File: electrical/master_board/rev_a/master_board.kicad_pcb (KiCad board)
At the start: 2 copper layers, 145.3 x 156.6 mm, 181 parts, among them CN1 USB3140-30-230-1-C;VERT,2.3FL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, CN10 WOW_OUT;M2x6S, CN2 USB3140-30-230-1-C;VERT,2.3FL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, CN5 LIDAR_ADAPTER;2xF1x3+F1x2, CN6 SERVO;F1x3, CN7 SERVO;F1x3, CN8 SERVO;F1x3, CN81 HCSR04LP;F1X4, CN82 HCSR04LP;F1X4, CN83 HCSR04LP;F1X4, CN84 HCSR04LP;F1X4, CN85 HCSR04LP;F1X4, CN86 HCSR04LP;F1X4, CN87 HCSR04LP;F1X4, CN88 MIKROBUS_MATE;SMALL, CN89 MIKROBUS_MATE;MEDIUM, CN9 SERVO;F1x3, CN90 STADAPTER;F2x4, CN91 HR2_ENCODER;2xF1x3, CN92 HR2_ENCODER;2xF1x3, CN93 POLOLU_U3V70F9;F1x4+F1x5, CN94 RASPI;F2X20, CN95 NUCLEO-F767ZI;2xF2x35, Q1 2N2222;SOT23, Q10 2N7000;SOT23, Q11 2N7000;SOT23, Q12 2N7000;SOT23, Q13 2N7000;SOT23, Q14 2N7000;SOT23, Q15 2N7000;SOT23, Q16 2N7000;SOT23, Q17 2N7000;SOT23, Q18 2N7000;SOT23, Q19 2N7000;SOT23, Q2 POWER_PFET_GSD, Q20 2N7000;SOT23, Q21 PFET_6A_GSD;SOT23, Q22 2N7000;SOT23, Q3 2N2222;SOT23, Q4 2N7000;SOT23, Q5 2N7000;SOT23, Q6 2N7000;SOT23, Q7 2N7000;SOT23, Q8 2N7000;SOT23, Q9 2N7000;SOT23, SW1 BUTTON;6x3.5, SW2 BUTTON;6x3.5, SW3 BUTTON;6x3.5, U1 LM66100;SOT363, U10 CD450B;TTSOP16, U11 SN74HCS595;TTSOP16, U12 SN74HCS595;TTSOP16, U13 74LVC1G11;SOT363, U14 MCP2542;SOIC8, U15 MCP2542;SOIC8, U16 74LVC1G74;TSSOP8, U17 CPC1017N;SOP4W3.8L4.1, U18 CPC1017N;SOP4W3.8L4.1, U2 MCP7940;SOIC8, U3 CAT24C32;SOIC8, U4 DRV8833PWPR;16HTSSOP, U5 SN74HCS595;TTSOP16, U6 SN74HCS166;TTSOP16, U7 SN74HCS166;TTSOP16, U8 SN74HCS595;TTSOP16, U9 CD450B;TTSOP16, X1 32.768kHz9pF;3.2x1.5

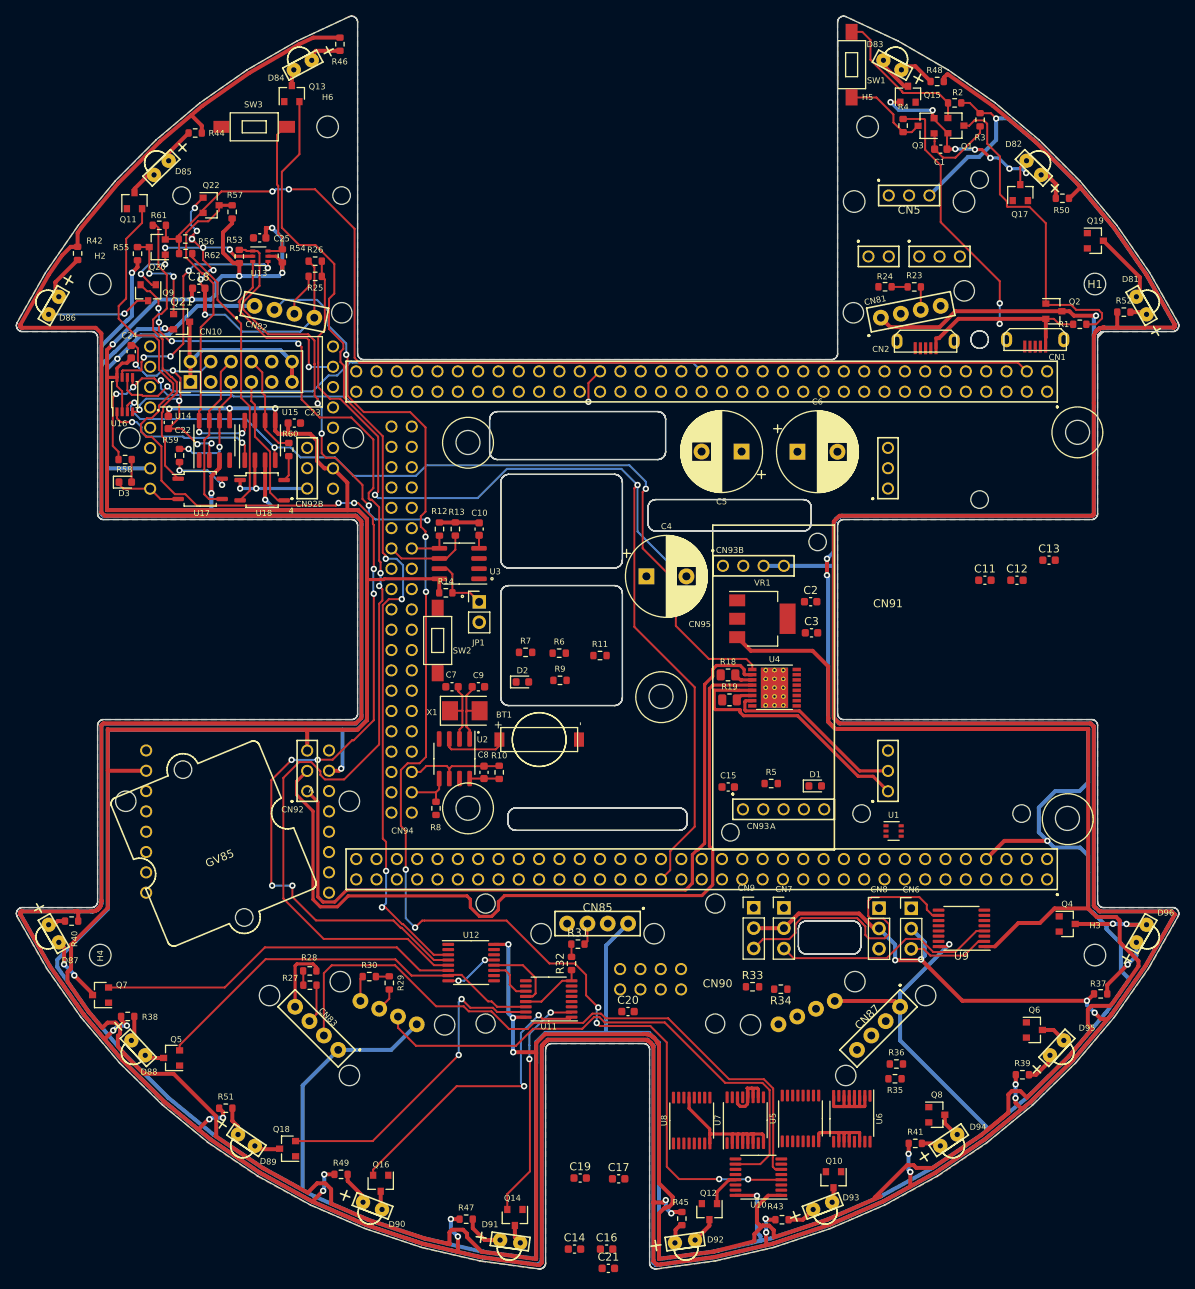
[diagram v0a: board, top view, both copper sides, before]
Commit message: More work on NW quadrant of PCB.
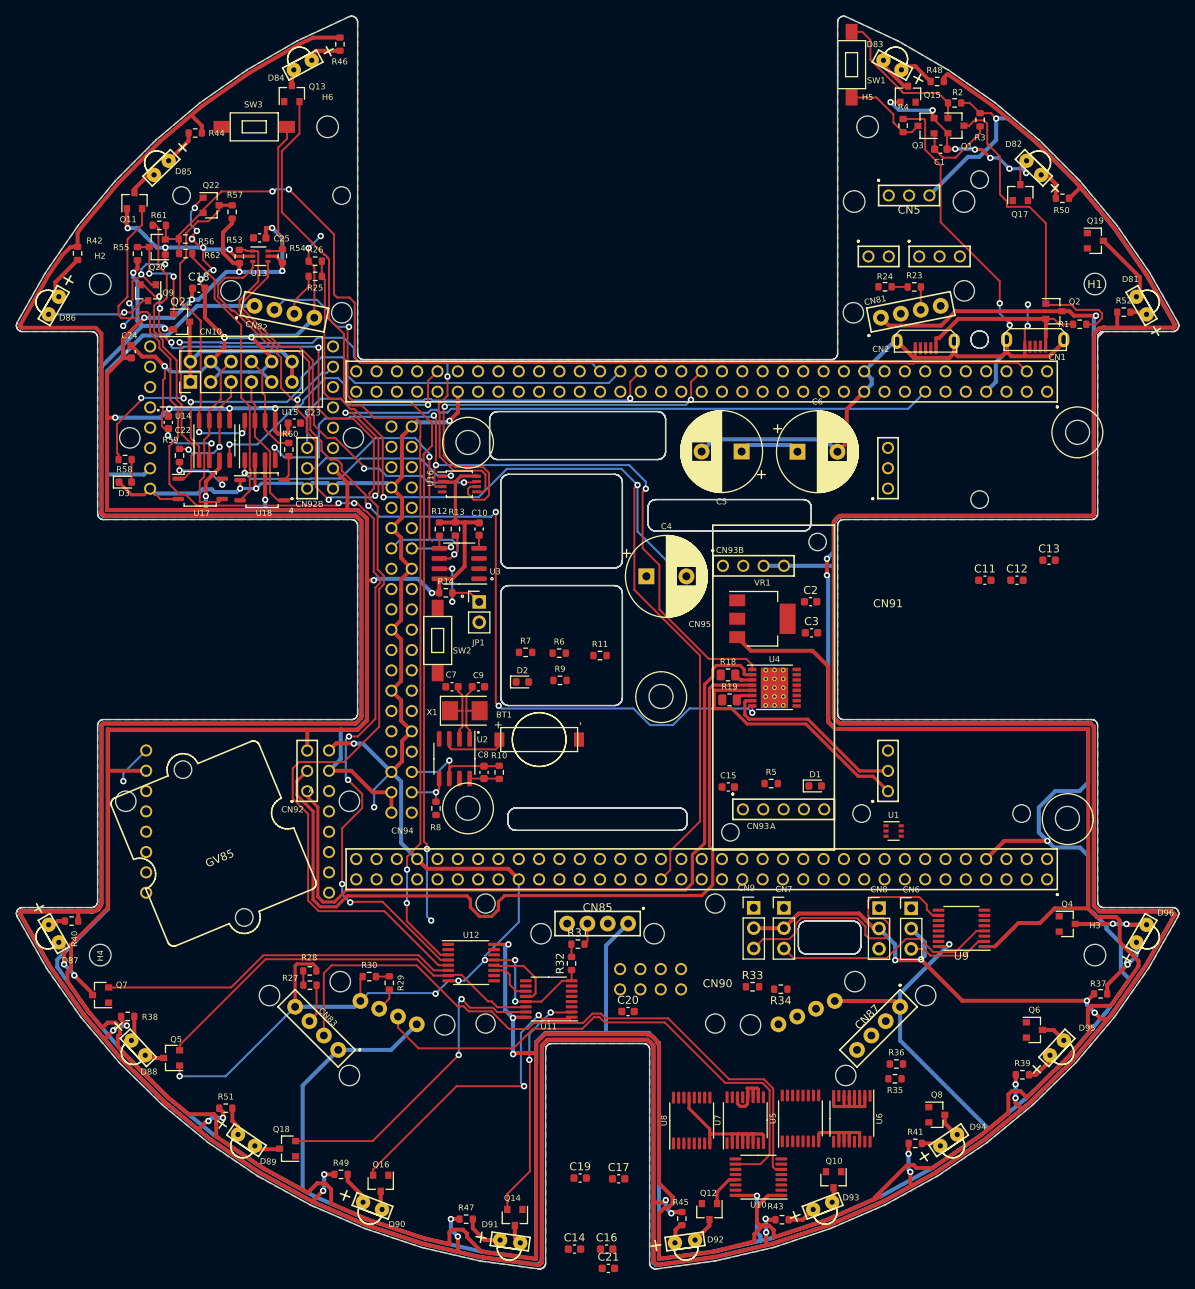
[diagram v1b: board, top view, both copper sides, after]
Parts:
- moved U16 43.3 mm to (82.7, 83.1), turned to 0 degrees
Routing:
- net /GND: track 228.4 -> 531.9 mm, vias 28 -> 42
- net /~NRST: track 23.6 -> 138.1 mm, vias 1 -> 4
- net /Sonars and Servos/TRIG2_5V: track 168.3 -> 95.4 mm, vias 9 -> 3
- net /WOW_TX: track 0.00 -> 67.4 mm, vias 0 -> 1
- net /~MOTOR_FAULT: track 53.8 -> 119.4 mm
- net /WOW_RX: track 0.00 -> 61.6 mm, vias 0 -> 2
- net /LQUAD_A: track 0.00 -> 28.8 mm, vias 0 -> 1
- net /LQUAD_B: track 0.00 -> 25.8 mm, vias 0 -> 1
- net /ESTOP: track 76.2 -> 98.8 mm
- net /~ESTOP_CLR: track 76.5 -> 55.7 mm, vias 1 -> 2
- net /WOWBus/~ESTOP_SET: track 31.2 -> 50.3 mm, vias 4 -> 2
- net /LED's/LED5: track 152.7 -> 138.0 mm, vias 8 -> 6
- net /5V: track 757.2 -> 767.9 mm, vias 11 -> 9
- net /WOWBus/ESTOP_TRIG: track 20.4 -> 30.8 mm
- net /~ESTOP: track 105.7 -> 95.7 mm, vias 3 -> 4
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
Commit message: More pushing and shoving of wires on PCB.
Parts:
- moved R7 7.67 mm to (83.4, 103.0)
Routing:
- net /DIO_MISO: track 0.00 -> 147.2 mm, vias 0 -> 3
- net /~DIO_NSS: track 0.00 -> 115.0 mm, vias 0 -> 4
- net /DIO_SCK: track 0.00 -> 104.4 mm, vias 0 -> 4
- net /ECHO7: track 2.01 -> 96.5 mm, vias 0 -> 4
- net /STL_TX: track 0.00 -> 74.9 mm, vias 0 -> 5
- net /SBC_ALIVE: track 0.00 -> 46.7 mm, vias 0 -> 2
- net /LQUAD_B: track 25.8 -> 66.4 mm
- net /GND: track 531.9 -> 559.4 mm
- net /DIO_MOSI: track 0.00 -> 26.4 mm, vias 0 -> 2
- net /ECHO2: track 134.0 -> 121.3 mm, vias 2 -> 4
- net /5V: track 767.9 -> 780.1 mm
- net /LED's/LED4: track 122.1 -> 126.3 mm, vias 2 -> 4
- net /~MOTOR_FAULT: track 119.4 -> 117.0 mm
- net /Motors_Encoders/LMOTOR_OUT2: track 102.4 -> 100.8 mm
- net /Single Board Computer/ID_SCL: track 15.0 -> 16.4 mm
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
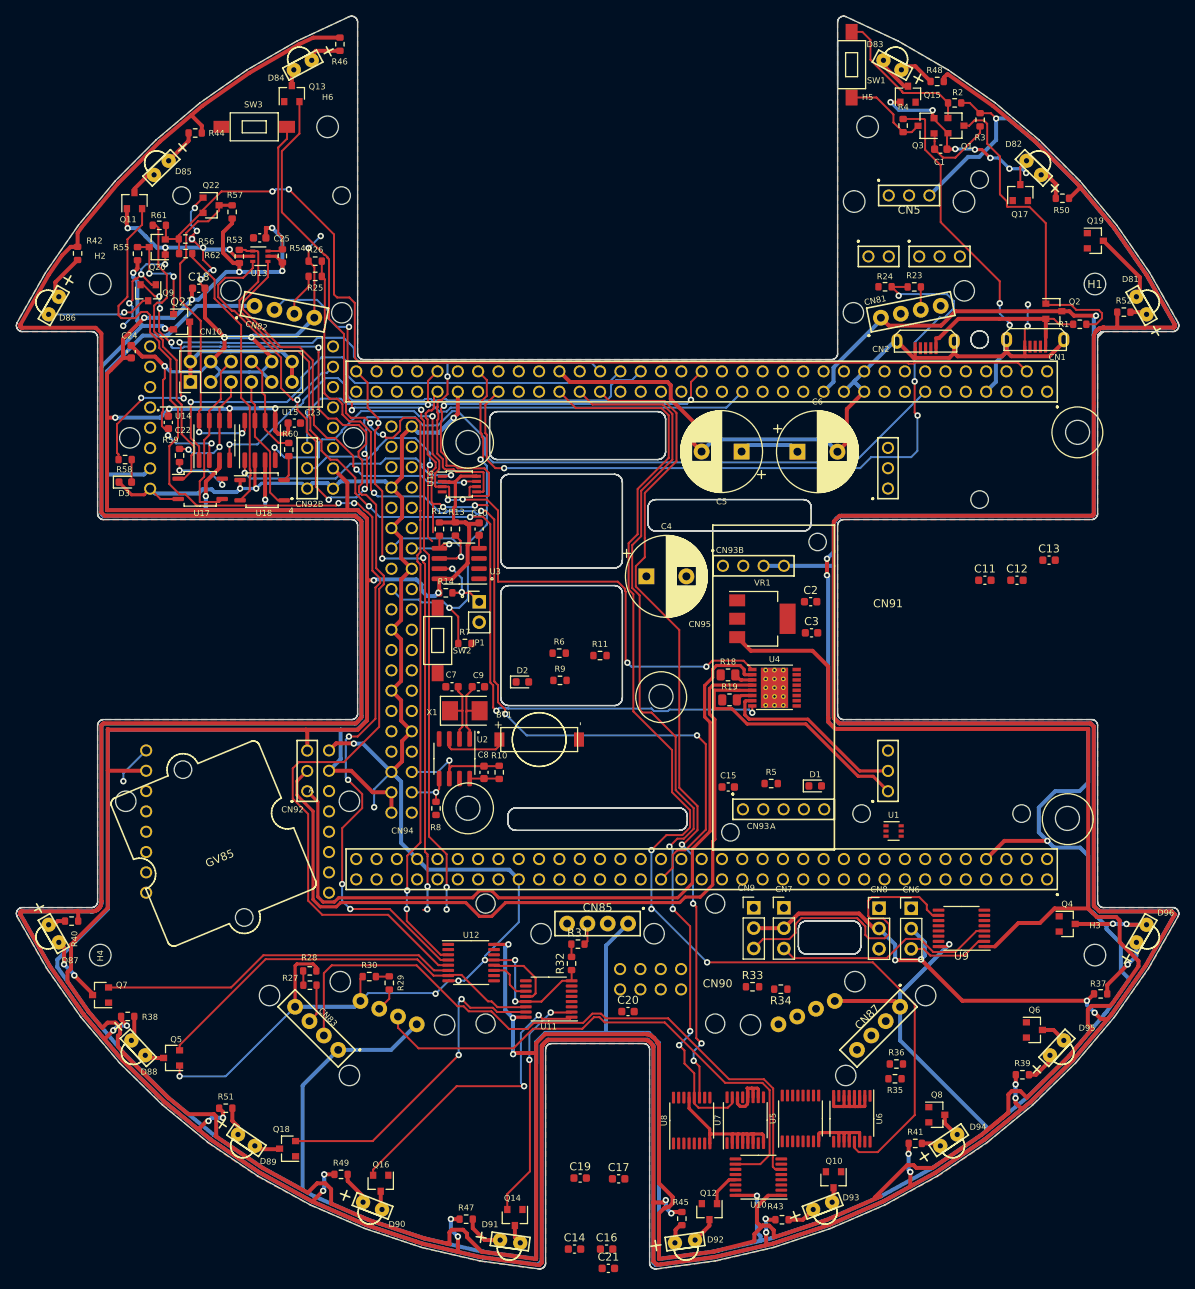
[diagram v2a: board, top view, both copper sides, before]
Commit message: Weaving traces from NE corner around the heat sink holes.
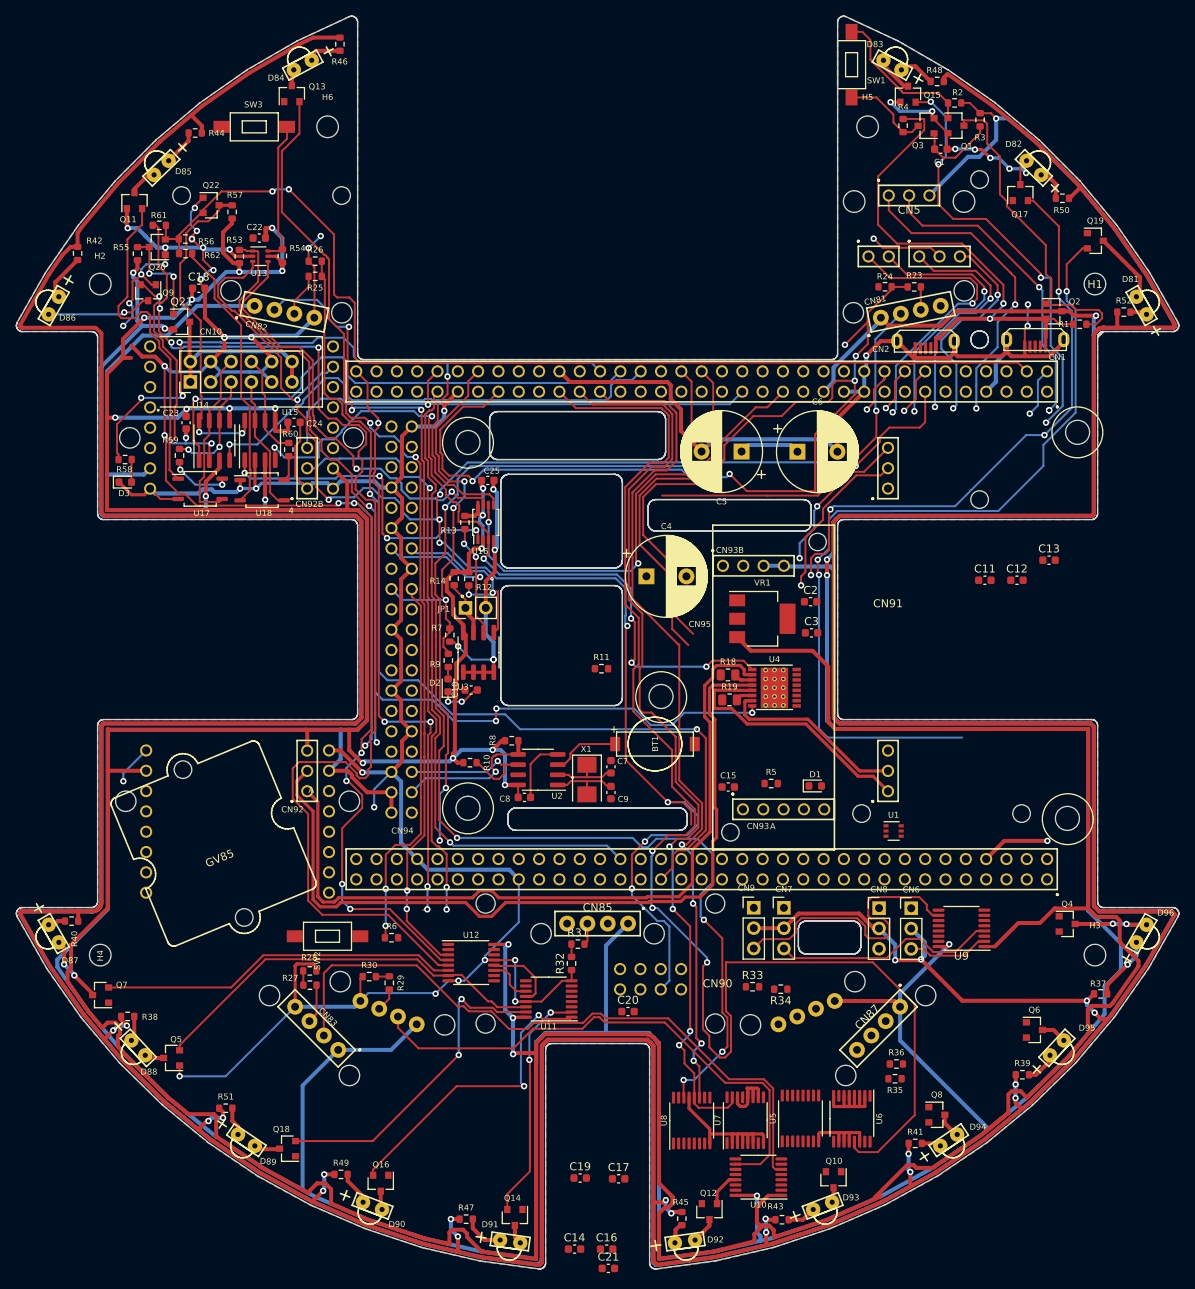
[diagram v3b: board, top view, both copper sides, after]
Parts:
- moved C25 41.6 mm to (86.3, 82.6), turned to 180 degrees
- moved R6 41.3 mm to (74.2, 139.8)
- moved SW2 39.5 mm to (66.2, 139.6), turned to 180 degrees
- moved C22 25.7 mm to (57.7, 52.3), turned to 0 degrees
- moved C7 22.2 mm to (101.7, 118.4), turned to 90 degrees
- moved C24 22.2 mm to (62.0, 75.3), turned to 180 degrees
- moved C9 21.2 mm to (101.7, 121.6), turned to 270 degrees
- moved C10 20.1 mm to (84.2, 108.8), turned to 180 degrees
- moved X1 17.5 mm to (98.7, 120.0), turned to 270 degrees
- moved BT1 14.5 mm to (107.2, 115.6)
- moved R9 14.2 mm to (81.3, 105.1), turned to 270 degrees
- moved C23 13.5 mm to (48.6, 75.4), turned to 90 degrees
- moved R8 12.7 mm to (89.3, 115.2), turned to 0 degrees
- moved U3 11.4 mm to (85.1, 104.1), turned to 90 degrees
- moved U2 10.5 mm to (92.5, 118.8), turned to 180 degrees
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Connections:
- C8 pad 2: /Single Board Computer/SBC_SCL -> /GND
- CN88 pad 11: /D11_PWM_MOSI -> Net-(CN88-Pad11)
- CN88 pad 12: /D12_MISO -> Net-(CN88-Pad12)
- CN88 pad 13: /D13_SCK -> Net-(CN88-Pad13)
- CN88 pad 14: /D10_PWM_NSS -> Net-(CN88-Pad14)
- CN88 pad 15: /~NRST -> Net-(CN88-Pad15)
- CN88 pad 16: /A1 -> Net-(CN88-Pad16)
- CN88 pad 3: /A4_SDA -> Net-(CN88-Pad3)
- CN88 pad 4: /A5_SCL -> Net-(CN88-Pad4)
- CN88 pad 5: /D0_RX -> Net-(CN88-Pad5)
- CN88 pad 6: /D1_TX -> Net-(CN88-Pad6)
- CN88 pad 7: /INT1 -> Net-(CN88-Pad7)
- CN89 pad 11: /D11_PWM_MOSI -> Net-(CN89-Pad11)
- CN89 pad 12: /D12_MISO -> Net-(CN89-Pad12)
- CN89 pad 13: /D13_SCK -> Net-(CN89-Pad13)
- CN89 pad 14: /D10_PWM_NSS -> Net-(CN89-Pad14)
- CN89 pad 15: /~NRST -> Net-(CN89-Pad15)
- CN89 pad 16: /A0 -> Net-(CN89-Pad16)
- CN89 pad 3: /A4_SDA -> Net-(CN89-Pad3)
- CN89 pad 4: /A5_SCL -> Net-(CN89-Pad4)
- CN89 pad 5: /D0_RX -> Net-(CN89-Pad5)
- CN89 pad 6: /D1_TX -> Net-(CN89-Pad6)
- CN89 pad 7: /INT0 -> Net-(CN89-Pad7)
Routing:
- net /LED's/LED1: track 0.00 -> 105.5 mm, vias 0 -> 3
- net /DIO_MOSI: track 26.4 -> 128.5 mm, vias 2 -> 4
- net /~NRST: track 138.5 -> 232.5 mm, vias 4 -> 10
- net /A4_SDA: track 0.00 -> 93.3 mm, vias 0 -> 4
- net /3.3V: track 641.3 -> 716.6 mm, vias 14 -> 21
- net /LED's/LED2: track 0.00 -> 74.0 mm, vias 0 -> 4
- net /GND: track 559.4 -> 625.9 mm, vias 42 -> 52
- net /ECHO7: track 96.5 -> 153.8 mm, vias 4 -> 5
- net /LQUAD_A: track 29.4 -> 86.3 mm, vias 1 -> 2
- net /LED's/LED3: track 0.00 -> 54.0 mm, vias 0 -> 4
- net /Single Board Computer/SBC_STOP: track 0.00 -> 47.0 mm, vias 0 -> 2
- net /Sonars and Servos/TRIG1_5V: track 0.00 -> 46.8 mm, vias 0 -> 1
- net /SERVO1: track 0.00 -> 45.7 mm
- net /Connectors/LDR_EN: track 0.00 -> 40.0 mm, vias 0 -> 2
- net /LDR_PWM: track 0.00 -> 38.8 mm, vias 0 -> 3
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
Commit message: Continue to work on PCB's.
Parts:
- removed C13: 10nF,16V,X7R;1608, Capacitor_SMD:C_0603_1608Metric
- C12: value 2.2uF,6.3V;1608 -> 2.2µF6.3V;1608
- CN81, CN82: footprint HR2:HCSR04_F1x4LP -> HR2:HCSR04_F1x4H
- CN83, CN87: footprint HR2:HCSR04_F1x4LP -> HR2:HCSR04_F1x4
- moved CN5 112.2 mm to (55.8, 126.2), turned to 270 degrees
- moved U1 69.9 mm to (153.0, 58.4)
- moved R11 54.8 mm to (57.8, 140.4)
- moved C6 44.0 mm to (145.5, 117.9), turned to 270 degrees
- moved C4 39.9 mm to (143.8, 81.6), turned to 90 degrees
- moved C12 29.0 mm to (125.1, 104.8), turned to 180 degrees
- moved C11 26.2 mm to (127.0, 110.2), turned to 270 degrees
- moved C5 18.7 mm to (111.0, 96.4)
- moved C3 4.19 mm to (126.0, 97.5), turned to 270 degrees
- moved C2 3.16 mm to (126.0, 100.9), turned to 90 degrees
- moved R34 1.99 mm to (124.7, 145.2)
- moved C15 1.71 mm to (117.8, 120.1)
- moved BT1 1.54 mm to (108.3, 116.6)
- moved VR1 0.68 mm to (120.3, 99.3), turned to 180 degrees
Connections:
- CN88 pad 15: Net-(CN88-Pad15) -> /~NRST
- CN89 pad 15: Net-(CN89-Pad15) -> /~NRST
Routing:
- net /GND: track 625.9 -> 1073.0 mm, vias 52 -> 67
- net /~LEDS_NSS: track 14.9 -> 152.7 mm, vias 1 -> 8
- net /LEDS_SCLK: track 12.0 -> 147.9 mm, vias 1 -> 7
- net /LED's/LED3: track 54.0 -> 184.1 mm, vias 4 -> 10
- net /Sonars and Servos/TRIG1_5V: track 46.8 -> 152.9 mm, vias 1 -> 8
- net /LED's/LED2: track 74.0 -> 170.9 mm, vias 4 -> 12
- net /SWCLK: track 5.58 -> 83.3 mm, vias 1 -> 4
- net /SWDIO: track 6.02 -> 81.1 mm, vias 1 -> 4
- net /A4_SDA: track 93.3 -> 167.8 mm, vias 4 -> 3
- net /SPBC_RX: track 0.00 -> 71.1 mm, vias 0 -> 1
- net /SPBC_TX: track 0.00 -> 65.4 mm, vias 0 -> 1
- net /SERVO1: track 45.7 -> 109.8 mm, vias 0 -> 2
- net /RQUAD_A: track 20.9 -> 78.3 mm, vias 1 -> 3
- net /RMOTOR_CTL1: track 0.00 -> 54.9 mm, vias 0 -> 3
- net /RQUAD_B: track 19.3 -> 73.9 mm, vias 2 -> 6
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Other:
- board text added: "CN91B"
